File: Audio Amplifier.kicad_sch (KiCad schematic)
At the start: 44 parts, among them J1 AudioJack3, J2 +12V 5A regulated power supply, J3 RIGHT_4ohm-SPEAKER, J4 LEFT_4ohm_SPEAKER, Q1 PMOS, SW1 SW_SPST, U1 TPA3110D2PWP

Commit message: Fix(ERC): Used KiCAD ERC to check the schematic and only found input pin not driven by output. Problem did not need resolving, meaning ERC ran clean
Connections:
- net at C2.1, L1.2: now also J4.+ (Pin_1); no longer J4.1 (Pin_1)
- net at C20.1, L2.2: now also J3.- (Pin_1); no longer J3.1 (Pin_1)
- net at C21.2, L3.2: now also J3.+ (Pin_2); no longer J3.2 (Pin_2)
- net at C3.2, L4.2: now also J4.- (Pin_2); no longer J4.2 (Pin_2)
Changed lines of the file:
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@@
 	)
 	(symbol
+		(lib_name "Conn_01x02_Socket_1")
 		(lib_id "Connector:Conn_01x02_Socket")
 		(at 222.25 76.2 0)
@@
 			)
 		)
-		(pin "2"
-		)
-		(pin "1"
+		(pin "+"
+		)
+		(pin "-"
 		)
 		(instances
@@
 	)
 	(symbol
+		(lib_name "Conn_01x02_Socket_2")
 		(lib_id "Connector:Conn_01x02_Socket")
 		(at 226.06 58.42 0)
@@
 			)
 		)
-		(pin "2"
-		)
-		(pin "1"
-		)
-		(instances
+		(pin "-"
+		)
+		(pin "+"
+		)
+		(instances

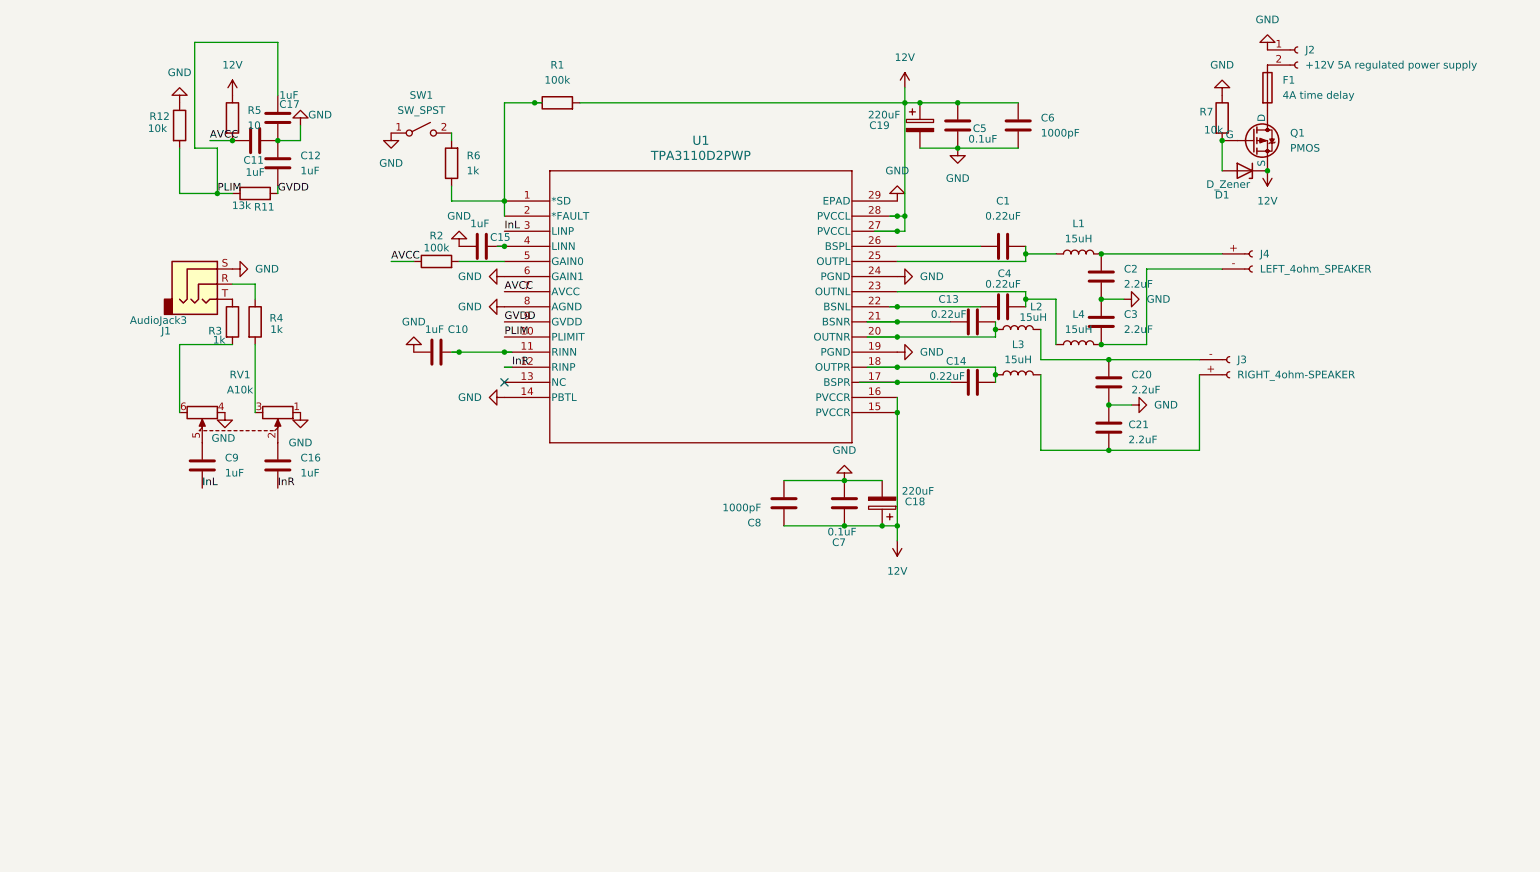
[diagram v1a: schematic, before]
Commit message: Feat(Footprints): Created a footprint library in the repo. Assigned initial footprints to all components, may be subject to change.
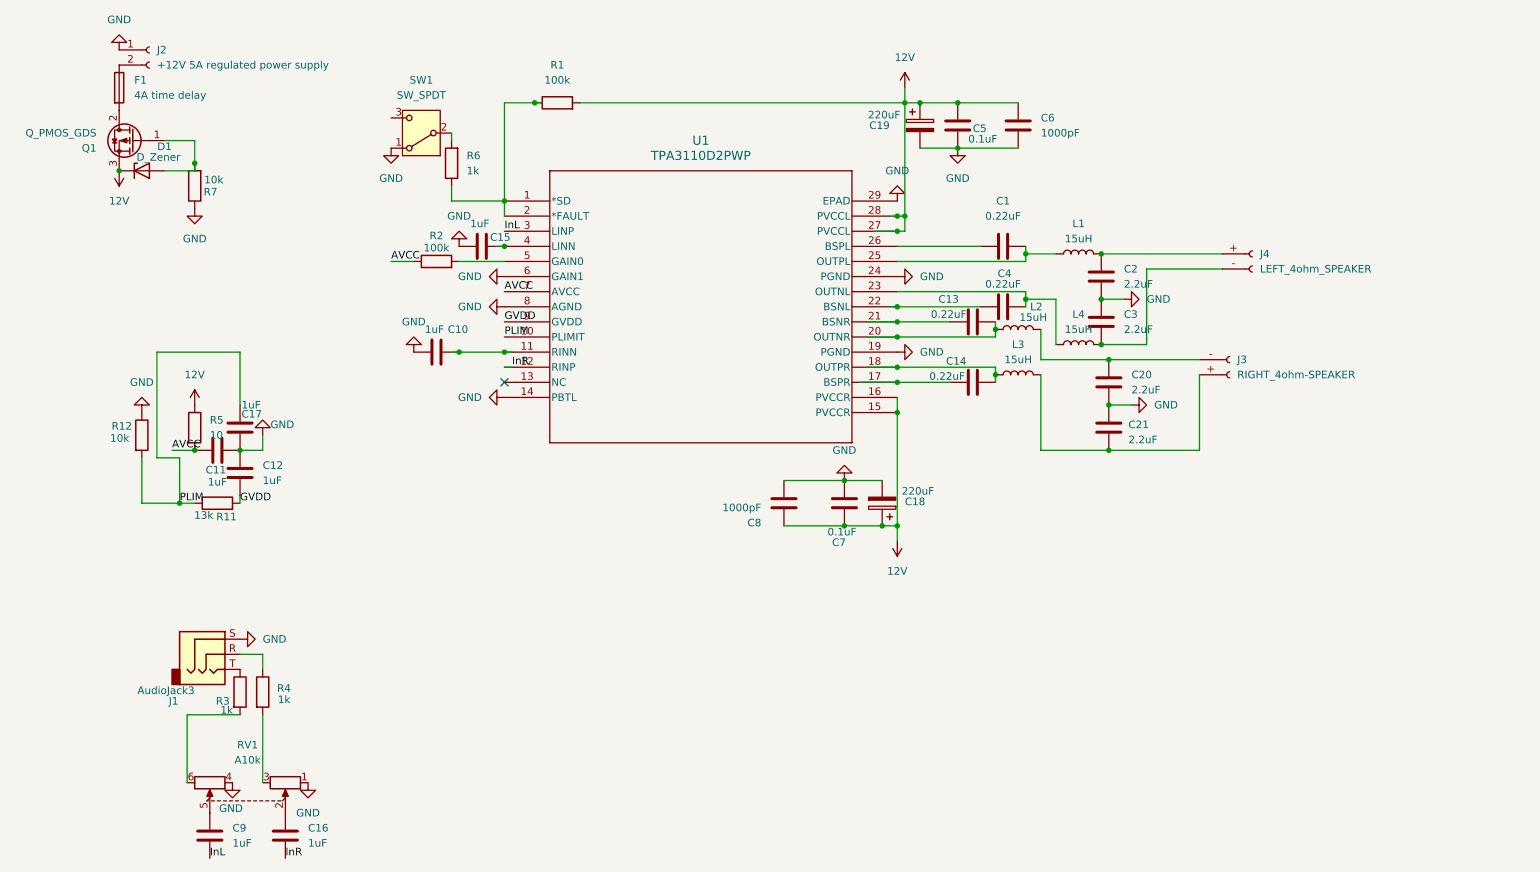
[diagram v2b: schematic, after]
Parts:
- removed Q1: PMOS, symbol Simulation_SPICE:PMOS
- removed SW1: SW_SPST, symbol Switch:SW_SPST
- added Q1: Q_PMOS_GDS, Package_TO_SOT_THT:TO-220-3_Vertical, symbol Transistor_FET:Q_PMOS_GDS
- added SW1: SW_SPDT, audio_amplifier:SPDT_OS102011_CNK, symbol Switch:SW_SPDT
- C1, C13, C14, C4, C5, C6, C7, C8: footprint (none) -> Capacitor_SMD:C_0805_2012Metric
- C10, C15, C16, C17, C9: footprint (none) -> Capacitor_THT:C_Rect_L7.2mm_W5.0mm_P5.00mm
- C11, C12: footprint (none) -> Capacitor_SMD:C_1206_3216Metric
- C18, C19: footprint (none) -> Capacitor_THT:CP_Radial_D8.0mm_P5.00mm
- C2, C20, C21, C3: footprint (none) -> audio_amplifier:CAP_C322C_MR_X7R_KEM
- D1: footprint (none) -> Diode_THT:D_DO-35_SOD27_P10.16mm_Horizontal
- F1: footprint (none) -> audio_amplifier:FUSRR508W60L840T400H810B
- J1: footprint (none) -> audio_amplifier:SJ1-3523N_CUD
- J2, J3, J4: footprint (none) -> audio_amplifier:CONN_1729128_PXC
- L1, L2, L3, L4: footprint (none) -> audio_amplifier:L_Wurth_WE-FAMI-8010_LeadDiameter0.5mm
- R1, R11, R12, R2, R3, R4, R5, R6, R7: footprint (none) -> Resistor_THT:R_Axial_DIN0207_L6.3mm_D2.5mm_P10.16mm_Horizontal
- RV1: footprint (none) -> audio_amplifier:PDB-182-K_20K_BRN
- U1: footprint PWP28_6P17X2P4 -> audio_amplifier:PWP28_6P17X2P4
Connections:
- net 12V: now also Q1.3 (S)
- net GND: now also SW1.1 (A)
- net at R6.2: now also SW1.2 (B)
- net at F1.2: now also Q1.2 (D)
- net at D1.2 (A), R7.2: now also Q1.1 (G)
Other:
- moved on the sheet: C11, C12, C16, C17, C9, D1, F1, J1, J2, R11, R12, R3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
